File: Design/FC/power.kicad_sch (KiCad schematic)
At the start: 59 parts, among them J1 XT60PW-M, U1 STM32H747BIT6, U2 INA219AIDCNT

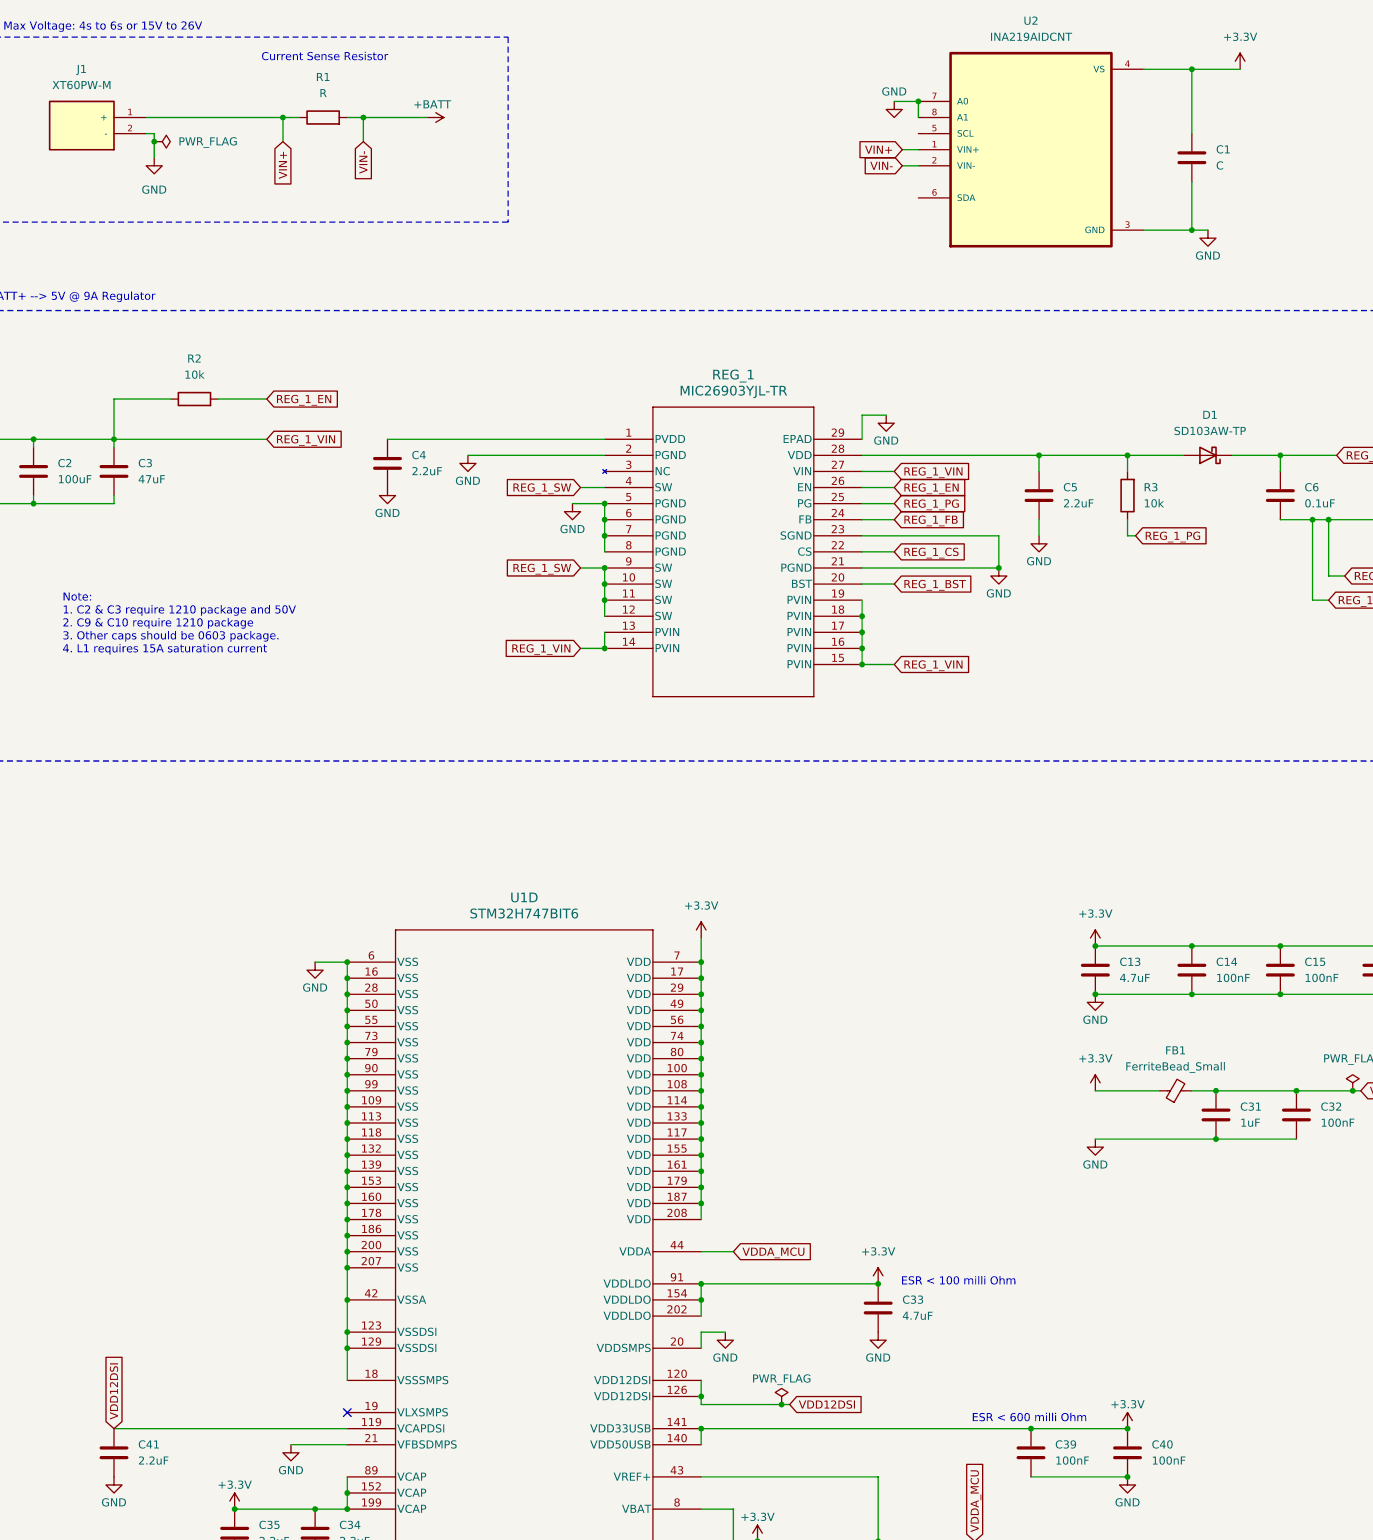
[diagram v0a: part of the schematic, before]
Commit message: added flash memory
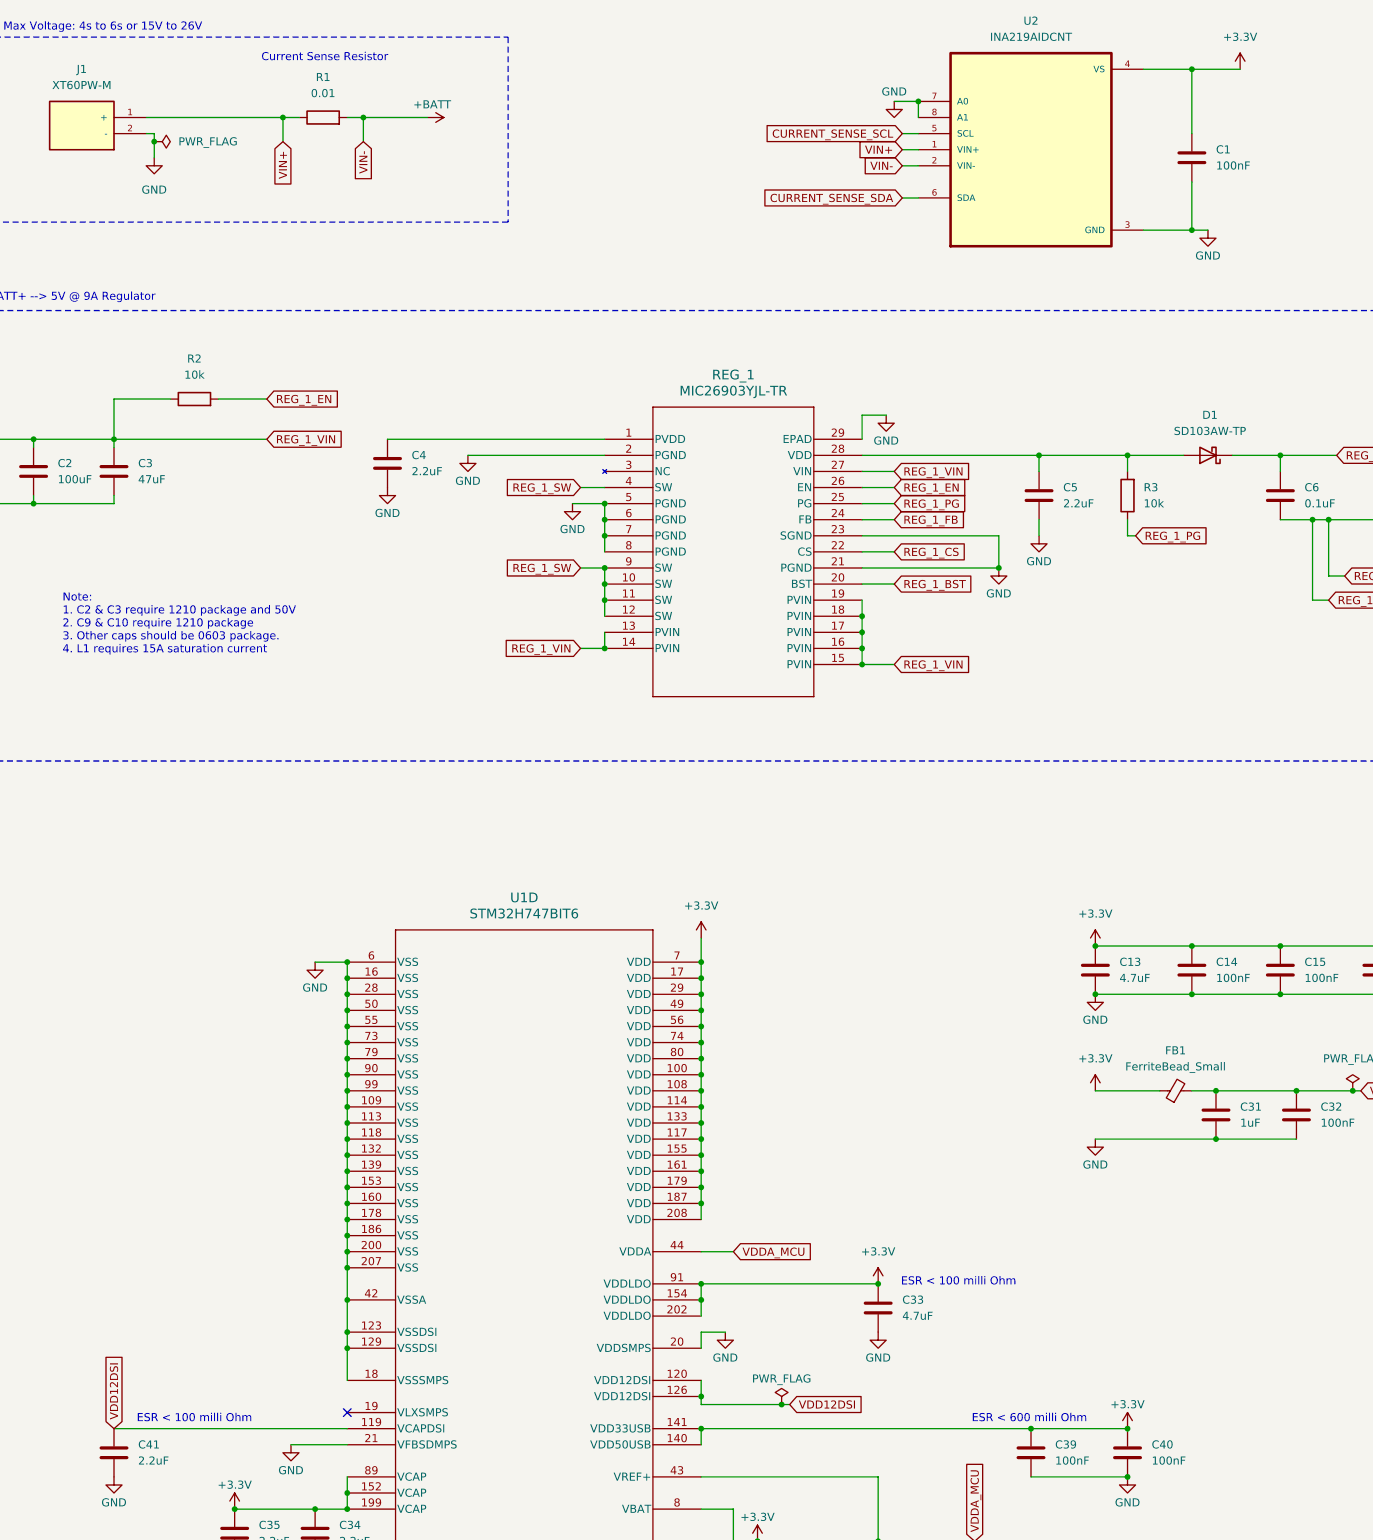
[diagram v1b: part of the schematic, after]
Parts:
- C1: value C -> 100nF
- FB1: footprint (none) -> Lib:MPZ1005S121HT000
- R1: value R -> 0.01; footprint (none) -> Lib:RES_PE2512_YAG
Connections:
- net CURRENT_SENSE_SCL: now reaches U2.5 (SCL)
- net CURRENT_SENSE_SDA: now reaches U2.6 (SDA)
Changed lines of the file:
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@@
 		)
 	)
+	(text "ESR < 100 milli Ohm"
+		(exclude_from_sim no)
+		(at 60.96 239.776 0)
+		(effects
+			(font
+				(size 1.27 1.27)
+			)
+		)
+	)
 	(text "Current Sense Resistor"
 		(exclude_from_sim no)
@@
 	(wire
 		(pts
+			(xy 172.72 36.83) (xy 175.26 36.83)
+		)
+		(stroke
+			(width 0)
+			(type default)
+		)
+	)
+	(wire
+		(pts
 			(xy 140.97 172.72) (xy 140.97 175.26)
 		)
@@
 	(wire
 		(pts
+			(xy 172.72 46.99) (xy 175.26 46.99)
+		)
+		(stroke
+			(width 0)
+			(type default)
+		)
+	)
+	(wire
+		(pts
 			(xy 218.44 26.67) (xy 226.06 26.67)
 		)
@@
 		)
 	)
+	(global_label "CURRENT_SENSE_SCL"
+		(shape input)
+		(at 172.72 36.83 180)
+		(fields_autoplaced yes)
+		(effects
+			(font
+				(size 1.27 1.27)
+			)
+			(justify right)
+		)
+		(property "Intersheetrefs" "${INTERSHEET_REFS}"
+			(at 149.6569 36.83 0)
+			(effects
+				(font
+					(size 1.27 1.27)
+				)
+				(justify right)
+				(hide yes)
+			)
+		)
+	)
 	(global_label "VIN+"
 		(shape input)
@@
 		)
 	)
+	(global_label "CURRENT_SENSE_SDA"
+		(shape input)
+		(at 172.72 46.99 180)
+		(fields_autoplaced yes)
+		(effects
+			(font
+				(size 1.27 1.27)
+			)
+			(justify right)
+		)
+		(property "Intersheetrefs" "${INTERSHEET_REFS}"
+			(at 149.5964 46.99 0)
+			(effects
+				(font
+					(size 1.27 1.27)
+				)
+				(justify right)
+				(hide yes)
+			)
+		)
+	)
 	(global_label "REG_1_SW"
 		(shape input)
@@
 			)
 		)
-		(property "Value" "R"
+		(property "Value" "0.01"
 			(at 81.28 30.48 90)
 			(effects
@@
 			)
 		)
-		(property "Footprint" ""
+		(property "Footprint" "Lib:RES_PE2512_YAG"
 			(at 81.28 36.068 90)
 			(effects
@@
 			)
 		)
-		(property "Footprint" ""
+		(property "Footprint" "Lib:MPZ1005S121HT000"
 			(at 215.9 189.738 90)
 			(effects
@@
 			)
 		)
-		(property "Value" "C"
+		(property "Value" "100nF"
 			(at 222.25 41.9099 0)
 			(effects

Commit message: started adding footprints and filling out bom
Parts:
- removed C11: 10uF, symbol Device:C
- removed C13, C33: 4.7uF, symbol Device:C
- removed C31: 1uF, symbol Device:C
- removed C7: 0.1uF, symbol Device:C
- removed C9: 100uF, symbol Device:C
- removed LED_2: G, symbol Device:LED
- removed R8: 240, symbol Device:R
- added C11, C31: 4.7uF, Capacitor_SMD:C_0603_1608Metric_Pad1.08x0.95mm_HandSolder, symbol Device:C_Polarized
- added C13: 1uF, Capacitor_SMD:C_0603_1608Metric_Pad1.08x0.95mm_HandSolder, symbol Device:C_Polarized
- added C50, C7, C9: 100uF, Lib:CAP_6.3 X 7.7_PAN, symbol CAP_6.3 X 7.7_PAN:EEE-FPV101XAP
- added C51: 2.2uF, Lib:CAP_C225K4REC7210_0805, symbol Device:C
- added LED_8: G, LED_SMD:LED_0603_1608Metric, symbol Device:LED
- added R20: 10k, Lib:RES_ERJ-T06J103V_0805, symbol Device:R
- C1, C12, C14, C15, C16, C17, C18, C19, C20, C21, C22, C23, C24, C25, C26, C27, C28, C29, C30, C32, C34, C35, C36, C37, C38, C39, C40, C41: footprint (none) -> Capacitor_SMD:C_0603_1608Metric_Pad1.08x0.95mm_HandSolder
- C10: value 100uF -> 10uF; footprint (none) -> Capacitor_SMD:C_0603_1608Metric_Pad1.08x0.95mm_HandSolder
- C2: value 100uF -> 22uF; footprint (none) -> Lib:CAP_GMK325BJ226MM-T-CAPC3225X280N
- C3: value 47uF -> 22uF; footprint (none) -> Lib:CAP_GMK325BJ226MM-T-CAPC3225X280N
- C4: footprint (none) -> Lib:CAP_C225K4REC7210_0805
- C5: value 2.2uF -> 0.1uF; footprint (none) -> Lib:CAP_C0805X104K5RAC3316_0805_100nF
- C6: footprint (none) -> Lib:CAP_C0805X104K5RAC3316_0805_100nF
- C8: footprint (none) -> Capacitor_SMD:C_0805_2012Metric_Pad1.18x1.45mm_HandSolder
- L1: value 5uH -> 6.8uH; footprint (none) -> Lib:IND_SRP1265A-6R8M_BRN
- LED_1: footprint (none) -> LED_SMD:LED_0603_1608Metric
- R2: footprint (none) -> Lib:RES_ERJ-T06J103V_0805
- R3: value 10k -> 240; footprint (none) -> Resistor_SMD:R_0603_1608Metric_Pad0.98x0.95mm_HandSolder
- R4: footprint (none) -> Lib:RES_ERJ-PB6B1962V_0805
- R5, R6: footprint (none) -> Resistor_SMD:R_0805_2012Metric_Pad1.20x1.40mm_HandSolder
- R7: footprint (none) -> Resistor_SMD:R_0603_1608Metric_Pad0.98x0.95mm_HandSolder
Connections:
- net +3.3V: now also C10.1, C11.1, C31.1, LED_8.2 (A)
- net +5V: now also C7.1, C9.1; no longer C10.1
- net +BATT: now also C50.1
- net GND: now also R3.1, C11.2, C13.2, C31.2, C50.2, C51.2, C7.2, C9.2; no longer C5.2
- net REG_1_CS: now also C5.1
- net REG_1_PG: now also R20.1; no longer R3.1
- net VDDA_MCU: now also C13.1
- net at R4.2: now also C5.2
- net at D1.2 (A), REG_1.28 (VDD): now also C51.1, R20.2; no longer C5.1, R3.2
- new net: LED_8.1 (K), R3.2

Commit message: started layout
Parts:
- added R59, R60, R63: 0, symbol Device:R_Small_US
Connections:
- net +BATT: now also R60.2, R63.1; no longer R1.2, REG_1.13 (PVIN), REG_1.14 (PVIN), REG_1.15 (PVIN), REG_1.16 (PVIN), REG_1.17 (PVIN), REG_1.18 (PVIN), REG_1.19 (PVIN), REG_1.27 (VIN), U2.2 (VIN-)
- net REG_1_CS: now also R59.2; no longer C6.2, REG_1.10 (SW), REG_1.11 (SW), REG_1.12 (SW), REG_1.4 (SW), REG_1.9 (SW)
- new net REG_1_SW: C6.2, R59.1, REG_1.10 (SW), REG_1.11 (SW), REG_1.12 (SW), REG_1.4 (SW), REG_1.9 (SW)
- new net REG_1_VIN: R63.2, REG_1.13 (PVIN), REG_1.14 (PVIN), REG_1.15 (PVIN), REG_1.16 (PVIN), REG_1.17 (PVIN), REG_1.18 (PVIN), REG_1.19 (PVIN), REG_1.27 (VIN)
- new net VIN-: R1.2, R60.1, U2.2 (VIN-)

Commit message: started laying out voltage regulator
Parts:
- removed R59, R60, R63: 0, symbol Device:R_Small_US
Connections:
- net +BATT is gone; now on net REG_1_VIN: C2.1, C3.1, C50.1, R2.1
- net REG_1_SW is gone; now on net REG_1_CS: C6.2, REG_1.10 (SW), REG_1.11 (SW), REG_1.12 (SW), REG_1.4 (SW), REG_1.9 (SW)
- net VIN- is gone; now on net REG_1_VIN: R1.2, U2.2 (VIN-)
- net REG_1_VDD: now reaches C51.1, D1.2 (A), R20.2, REG_1.28 (VDD)
- net REG_1_PVDD: now reaches C4.1, REG_1.1 (PVDD)

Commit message: before shrinking pcb
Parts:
- added H1, H3: MountingHole, MountingHole:MountingHole_3.2mm_M3_Pad_Via, symbol Mechanical:MountingHole_Pad
- added H2, H4: MountingHole_Pad, MountingHole:MountingHole_3.2mm_M3_Pad_Via, symbol Mechanical:MountingHole_Pad
- added NT1, NT2, NT3, NT4, NT5, NT6: NT, Lib:NetTie-2_SMD_Track0.35mm, symbol Device:NetTie_2
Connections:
- net +3.3V: now also NT1.1, NT2.2, NT4.1, NT6.1; no longer C31.1, C34.1, C35.1, C36.1, C39.1, C40.1, U1.140 (VDD50USB), U1.141 (VDD33USB), U1.152 (VCAP), U1.154 (VDDLDO), U1.199 (VCAP), U1.202 (VDDLDO), U1.8 (VBAT), U1.89 (VCAP), U1.91 (VDDLDO)
- net GND: now also H1.1, H2.1, H3.1, H4.1
- net VDD12DSI: now also NT3.2; no longer C41.1, U1.119 (VCAPDSI)
- net VDDA_MCU: now also NT5.1; no longer C37.1, C38.1, U1.43 (VREF+)
- new net VBAT: C36.1, NT6.2, U1.8 (VBAT)
- new net VCAP: C34.1, C35.1, NT2.1, U1.152 (VCAP), U1.199 (VCAP), U1.89 (VCAP)
- new net VCAPDSI: C41.1, NT3.1, U1.119 (VCAPDSI)
- new net VDDUSB: C39.1, C40.1, NT4.2, U1.140 (VDD50USB), U1.141 (VDD33USB)
- new net VDD_LDO: C31.1, NT1.2, U1.154 (VDDLDO), U1.202 (VDDLDO), U1.91 (VDDLDO)
- new net VREF+: C37.1, C38.1, NT5.2, U1.43 (VREF+)
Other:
- note added: "Mounting Holes"
- moved on the sheet: C36, C37, C38

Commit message: finished pcb layout and started on bom
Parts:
- C1, C14, C15, C16, C17, C18, C19, C20, C21, C22, C23, C24, C25, C26, C27, C28, C29, C30, C32, C36, C37, C39, C40: Manufacturer_Name (none) -> YAGEO; Manufacturer_Part_Number (none) -> CC0603KRX7R7BB104; PACKAGE_TYPE (none) -> SMD 0603
- C10, C12: Manufacturer_Name (none) -> Murata Electronics; Manufacturer_Part_Number (none) -> GRM188R61E106KA73D; PACKAGE_TYPE (none) -> SMD 0603
- C11, C31: Manufacturer_Name (none) -> Murata Electronics; Manufacturer_Part_Number (none) -> GRM188R61E475KE11D; PACKAGE_TYPE (none) -> SMD 0603
- C13: Manufacturer_Name (none) -> KYOCERA AVX; Manufacturer_Part_Number (none) -> TACL105K016RTA; PACKAGE_TYPE (none) -> SMD 0603
- C2, C3: footprint Lib:CAP_GMK325BJ226MM-T-CAPC3225X280N -> Capacitor_SMD:C_1210_3225Metric_Pad1.33x2.70mm_HandSolder; Manufacturer_Name (none) -> Taiyo Yuden; Manufacturer_Part_Number (none) -> MSASG32MSB5226MPNA01; PACKAGE_TYPE (none) -> SMD 1210
- C34, C35, C41: Manufacturer_Name (none) -> Taiyo Yuden; Manufacturer_Part_Number (none) -> TMK107ABJ225KA-T; PACKAGE_TYPE (none) -> SMD 0603
- C38: Manufacturer_Name (none) -> Murata Electronics; Manufacturer_Part_Number (none) -> GRM188R61A105KA61D; PACKAGE_TYPE (none) -> SMD 0603
- C4, C51: footprint Lib:CAP_C225K4REC7210_0805 -> Capacitor_SMD:C_0805_2012Metric_Pad1.18x1.45mm_HandSolder; Manufacturer_Name (none) -> Taiyo Yuden; Manufacturer_Part_Number (none) -> UMK212BB7225KG-T; PACKAGE_TYPE (none) -> SMD 0805
- C5, C6: footprint Lib:CAP_C0805X104K5RAC3316_0805_100nF -> Capacitor_SMD:C_0805_2012Metric_Pad1.18x1.45mm_HandSolder; Manufacturer_Name (none) -> KYOCERA AVX; Manufacturer_Part_Number (none) -> KGM21NR71H104KT; PACKAGE_TYPE (none) -> SMD 0805
- C50, C7, C9: Manufacturer_Name (none) -> Panasonic Electronic Components; Manufacturer_Part_Number (none) -> EEE-FPV101XAP; PACKAGE_TYPE (none) -> 6.60mm x 6.60mm
- C8: Manufacturer_Name (none) -> KEMET; Manufacturer_Part_Number (none) -> C0805C472J3GEC7210; PACKAGE_TYPE (none) -> SMD 0805
- D1: footprint Lib:SD103AW-TP-SODFL1608X70N -> Diode_SMD:Nexperia_CFP3_SOD-123W; Manufacturer_Name (none) -> MCC (Micro Commercial Components); Manufacturer_Part_Number (none) -> SD103AW-TP; PACKAGE_TYPE (none) -> SOD123
- FB1: Manufacturer_Name (none) -> TDK Corporation; Manufacturer_Part_Number (none) -> MPZ1005S121HT000; PACKAGE_TYPE (none) -> SMD 0402
- J1: Manufacturer_Name (none) -> AMASS; Manufacturer_Part_Number (none) -> XT60PW-M; PACKAGE_TYPE (none) -> THT Right Angle
- L1: Manufacturer_Name (none) -> Bourns Inc.; Manufacturer_Part_Number (none) -> SRP1265A-6R8M; PACKAGE_TYPE (none) -> SMD MOHM
- LED1: renamed from LED_1; Manufacturer_Name (none) -> Dialight; Manufacturer_Part_Number (none) -> 5990081007F; PACKAGE_TYPE (none) -> SMD 0603
- LED8: renamed from LED_8; Manufacturer_Name (none) -> Dialight; Manufacturer_Part_Number (none) -> 5990081007F; PACKAGE_TYPE (none) -> SMD 0603
- REG_2: footprint Lib:LD39200PU33R-SON95P300X300X100-7N -> Regulators:SON95P300X300X100-7N
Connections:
- net GND: now also REG_1.32 (GND)
- net REG_1_CS: now also REG_1.30 (SW)
- net REG_1_VIN: now also REG_1.31 (PVIN)
